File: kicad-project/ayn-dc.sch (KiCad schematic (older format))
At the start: 27 parts, among them J2 Si5351_Module, J3 BluePill_Left, J4 BluePill_Right, K1 G6K-2F-Y, Q1 MMBT3904, U1 L7805, U2 24LC64

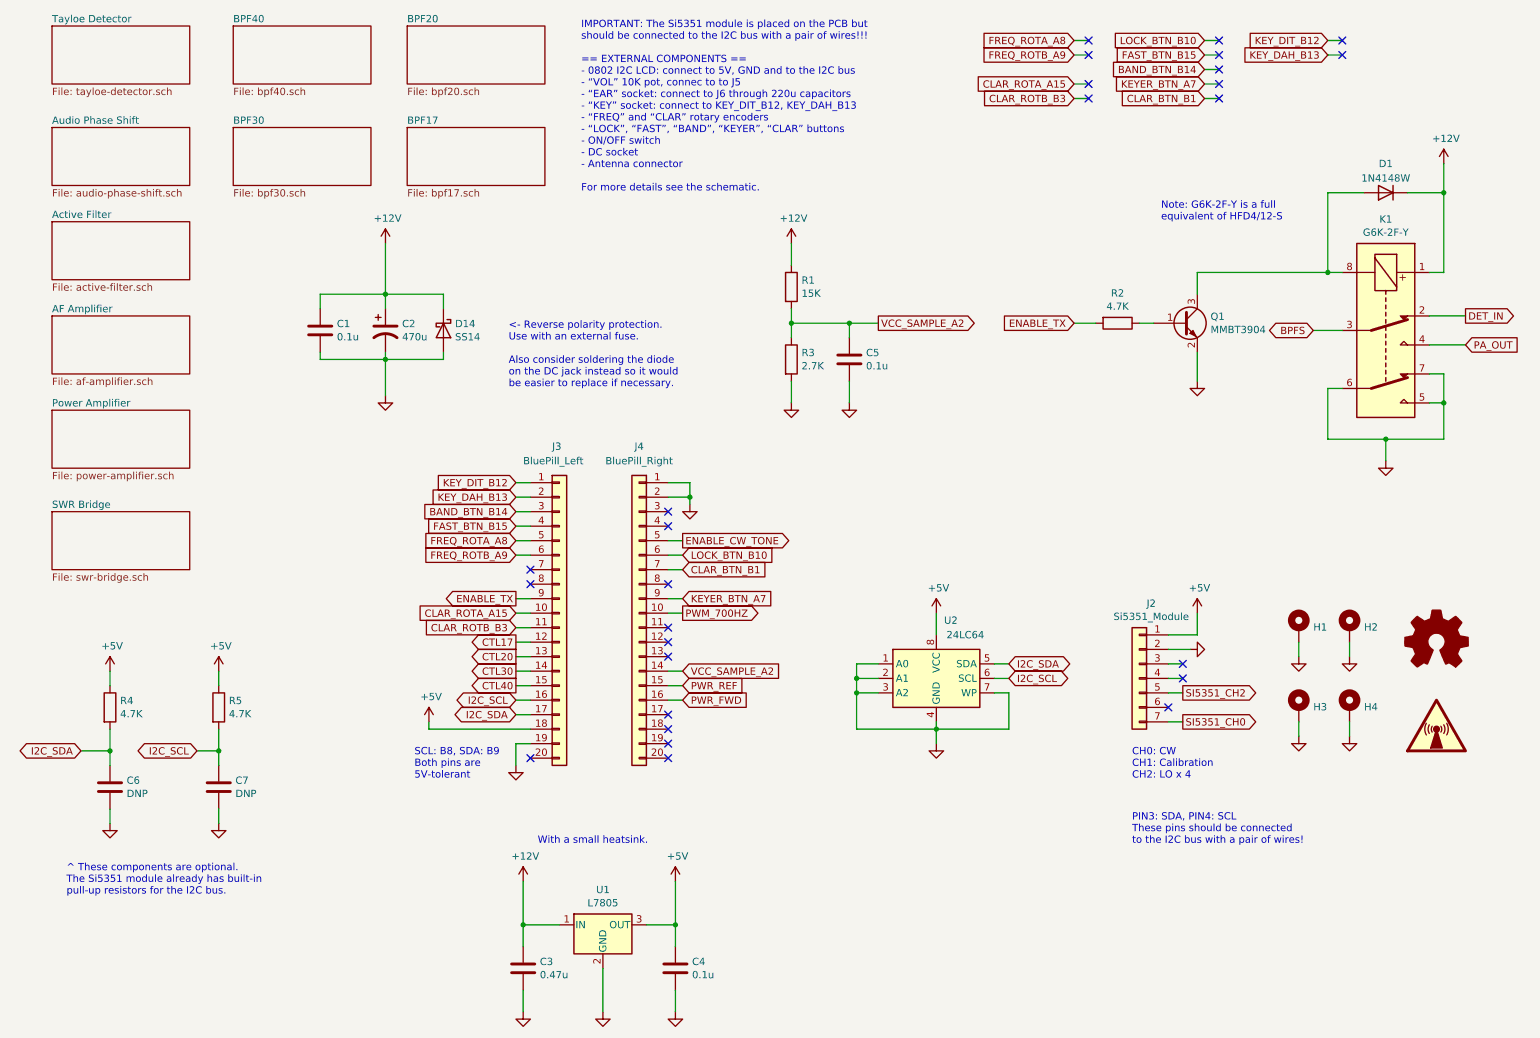
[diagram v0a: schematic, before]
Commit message: HW: use 5V_DIGITAL and move I2C away from 5V bus
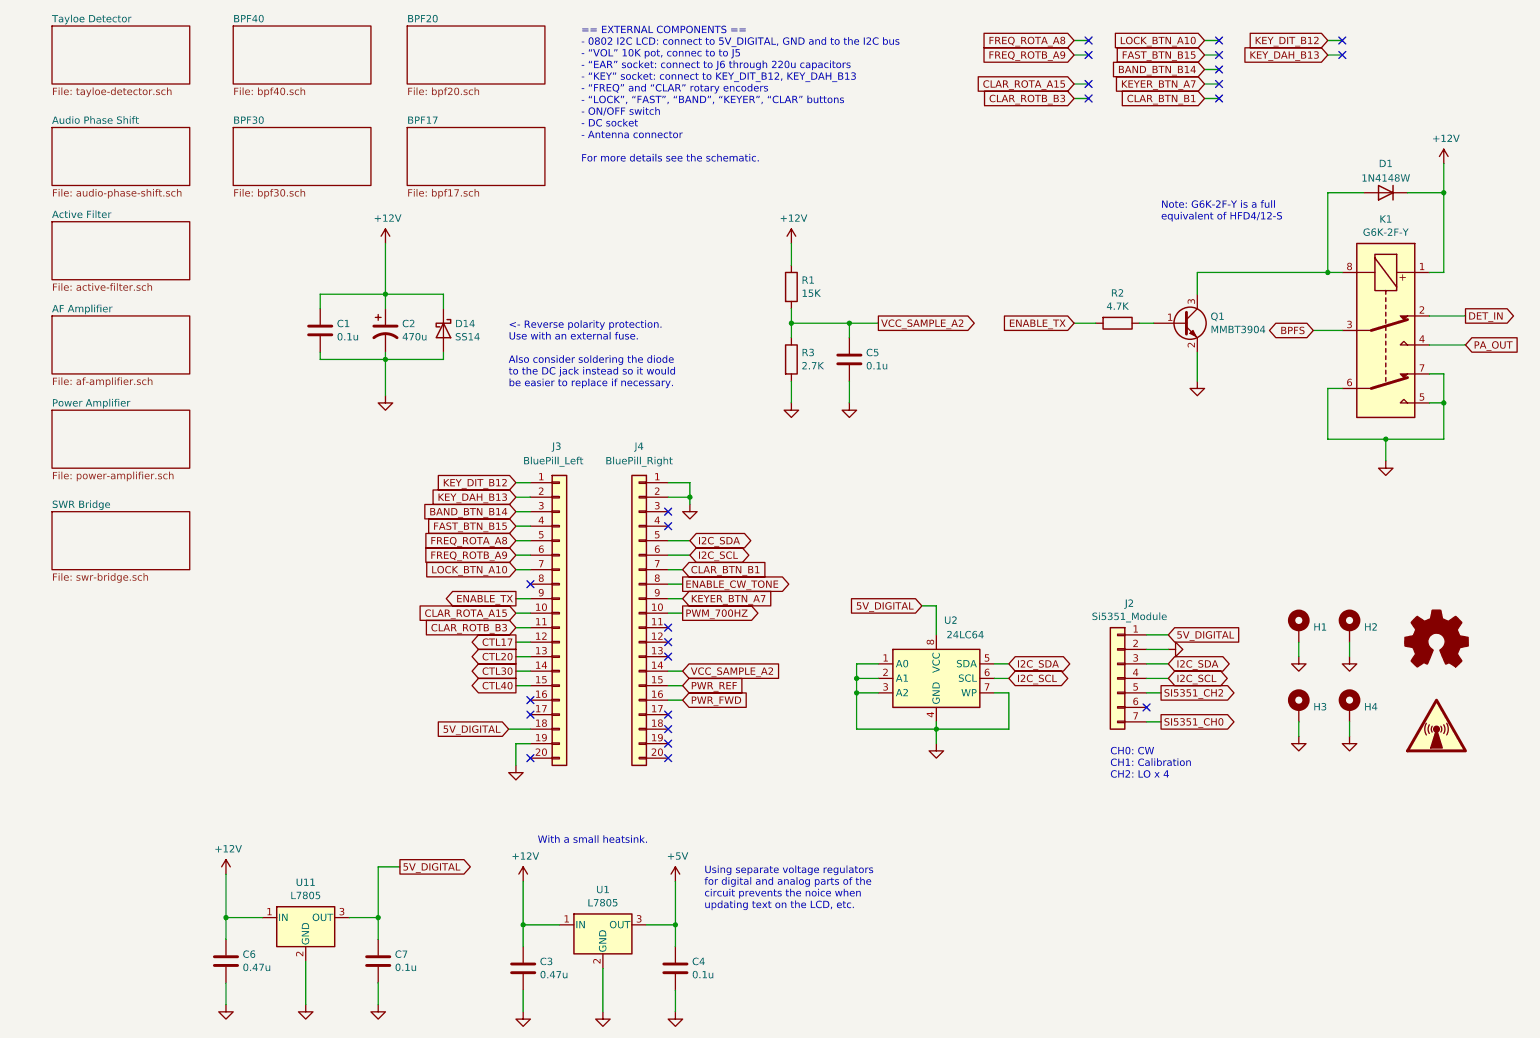
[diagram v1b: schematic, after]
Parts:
- removed R4, R5: 4.7K, Resistor_SMD:R_0805_2012Metric_Pad1.15x1.40mm_HandSolder, symbol Device:R
- added U11: L7805, Package_TO_SOT_SMD:TO-263-2, symbol Regulator_Linear:L7805
- C6: value DNP -> 0.47u
- C7: value DNP -> 0.1u
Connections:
- net LOCK_BTN_B10 is gone; now on net I2C_SCL: J4.6 (Pin_6)
- net +12V: now also C6.1, U11.1 (IN)
- net +5V: no longer J2.1 (Pin_1), J3.18 (Pin_18), U2.8 (VCC)
- net ENABLE_CW_TONE: now also J4.8 (Pin_8); no longer J4.5 (Pin_5)
- net GND: now also U11.2 (GND)
- net I2C_SCL: now also J2.4 (Pin_4); no longer C7.1, J3.16 (Pin_16)
- net I2C_SDA: now also J2.3 (Pin_3), J4.5 (Pin_5); no longer C6.1, J3.17 (Pin_17)
- net LOCK_BTN_A10: now reaches J3.7 (Pin_7)
- new net 5V_DIGITAL: C7.1, J2.1 (Pin_1), J3.18 (Pin_18), U11.3 (OUT), U2.8 (VCC)
- no-connect marks 27 -> 25
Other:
- note added: "<- Reverse polarity protection.\nUse with an external fuse.\n\nAlso consider soldering the diode\nto the DC jack instead so it would\nbe easier to replace if necessary."
- note added: "== EXTERNAL COMPONENTS ==\n- 0802 I2C LCD: connect to 5V_DIGITAL, GND and to the I2C bus\n- “VOL” 10K pot, connec to to J5\n- “EAR” socket: connect to J6 through 220u capacitors\n- “KEY” socket: connect to KEY_DIT_B12, KEY_DAH_B13\n- “FREQ” and “CLAR” rotary encoders\n- “LOCK”, “FAST”, “BAND”, “KEYER”, “CLAR” buttons\n- ON/OFF switch\n- DC socket\n- Antenna connector\n\nFor more details see the s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"
- note added: "Using separate voltage regulators\nfor digital and analog parts of the\ncircuit prevents the noice when\nupdating text on the LCD, etc."
- note removed: "<- Reverse polarity protection.\nUse with an external fuse.\n\nAlso consider soldering the diode\non the DC jack instead so it would\nbe easier to replace if necessary."
- note removed: "IMPORTANT: The Si5351 module is placed on the PCB but\nshould be connected to the I2C bus with a pair of wires!!!\n\n== EXTERNAL COMPONENTS ==\n- 0802 I2C LCD: connect to 5V, GND and to the I2C bus\n- “VOL” 10K pot, connec to to J5\n- “EAR” socket: connect to J6 through 220u capacitors\n- “KEY” socket: connect to KEY_DIT_B12, KEY_DAH_B13\n- “FREQ” and “CLAR” rotary encoders\n- “LOCK”, “FAST”, “BA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"
- note removed: "PIN3: SDA, PIN4: SCL\nThese pins should be connected\nto the I2C bus with a pair of wires!"
- note removed: "SCL: B8, SDA: B9\nBoth pins are \n5V-tolerant"
- note removed: "^ These components are optional.\nThe Si5351 module already has built-in\npull-up resistors for the I2C bus."
- moved on the sheet: J2
